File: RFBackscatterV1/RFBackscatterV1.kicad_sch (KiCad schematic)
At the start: 3 parts, among them J1 SMA-J-P-H-RA-TH1, U1 HSWA2-30DR+

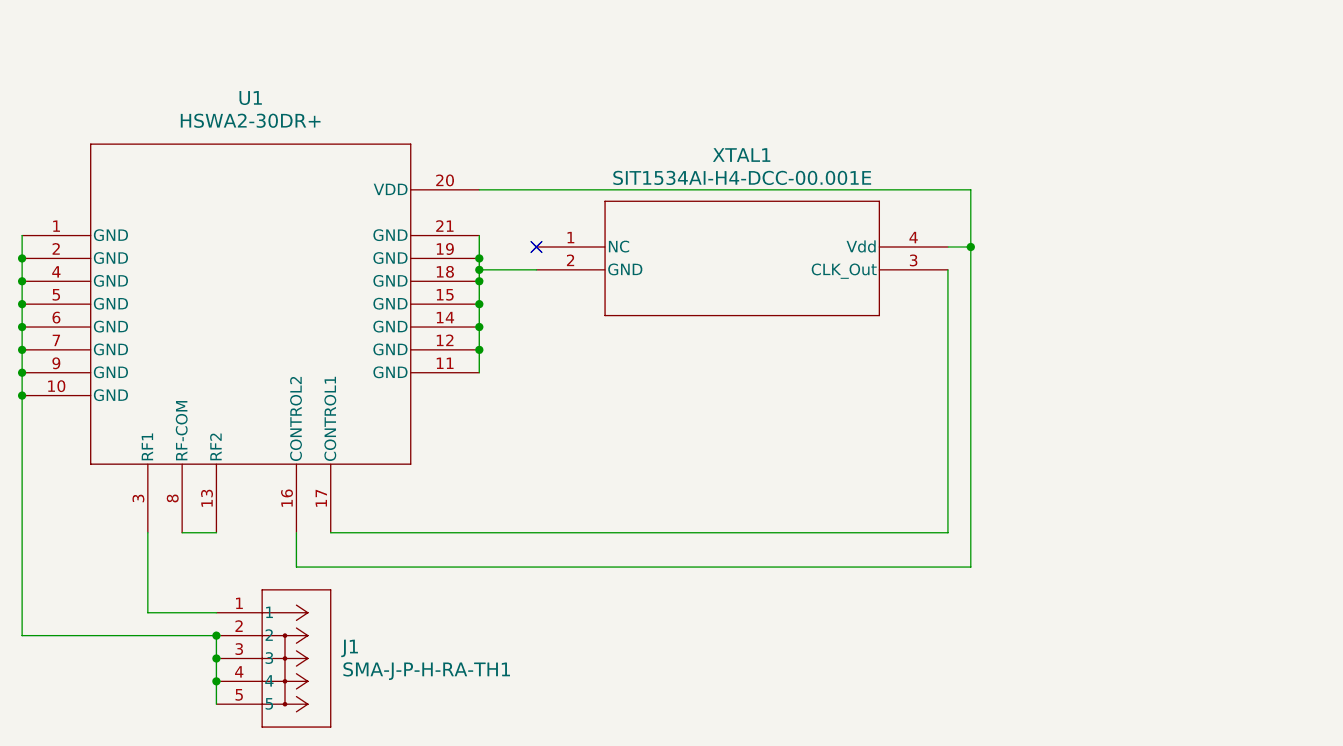
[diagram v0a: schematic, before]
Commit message: Added SKY13351, finished initial schematic
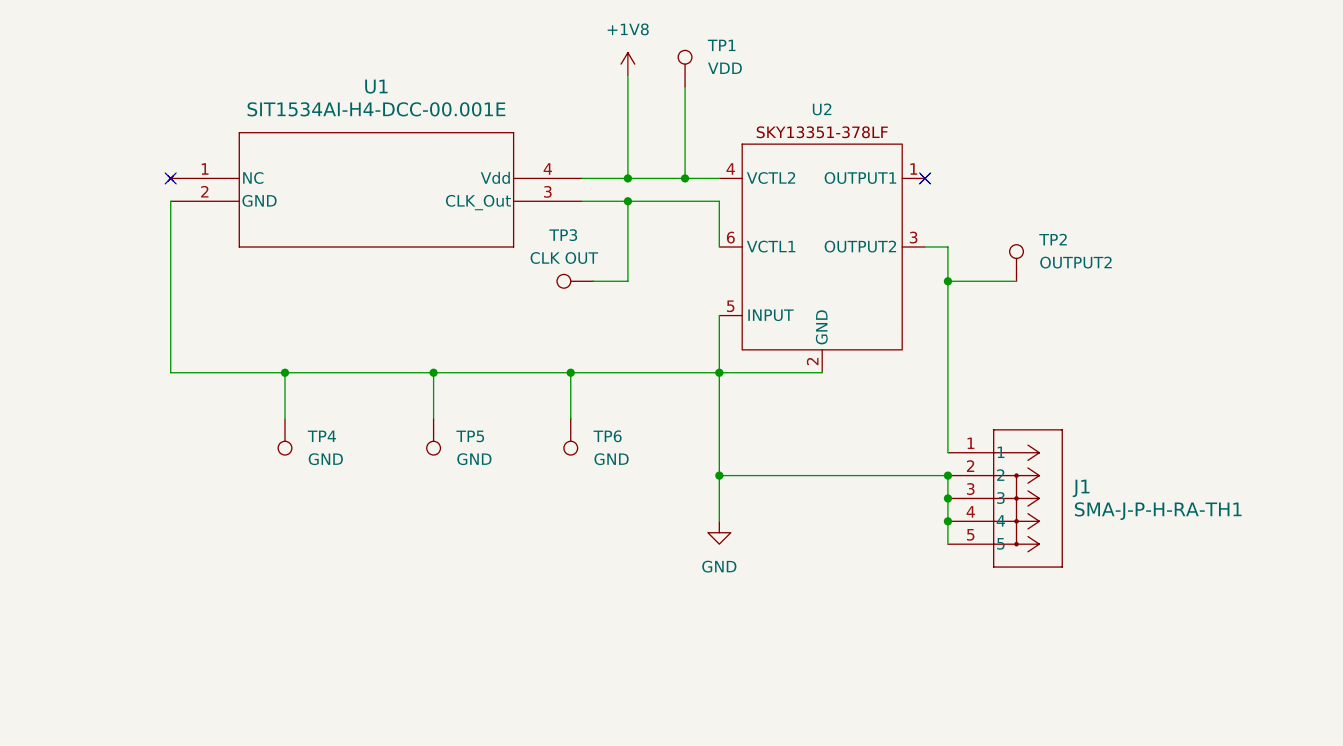
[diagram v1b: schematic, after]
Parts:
- removed U1: HSWA2-30DR+, DG983-1_MNC, symbol 2024-02-16_20-57-40:HSWA2-30DR+
- added TP1: VDD, symbol Connector:TestPoint
- added TP2: OUTPUT2, symbol Connector:TestPoint
- added TP3: CLK OUT, symbol Connector:TestPoint
- added TP4, TP5, TP6: GND, symbol Connector:TestPoint
- added U2: ~, symbol WADAR_KiCAD_Library:SKY13351-378LF
- renumbered XTAL1 to U1
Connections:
- net GND: now reaches U1.2 (GND)
- net GND: now also J1.2, J1.3, J1.4, J1.5, TP4.1, TP5.1, TP6.1, U2.2 (GND), U2.5 (INPUT)
- net at U1.3 (CLK_Out): now also TP3.1, U2.6 (VCTL1)
- net +1V8: now reaches U1.4 (Vdd)
- net +1V8: now also TP1.1, U2.4 (VCTL2)
- net at J1.1: now also TP2.1, U2.3 (OUTPUT2)
- no-connect marks 1 -> 2
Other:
- company: (none) -> UCSC J-Lab
- title: (none) -> RF Backscatter Tag
- moved on the sheet: J1, U1

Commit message: Finished SKY13351 footprint, staged board
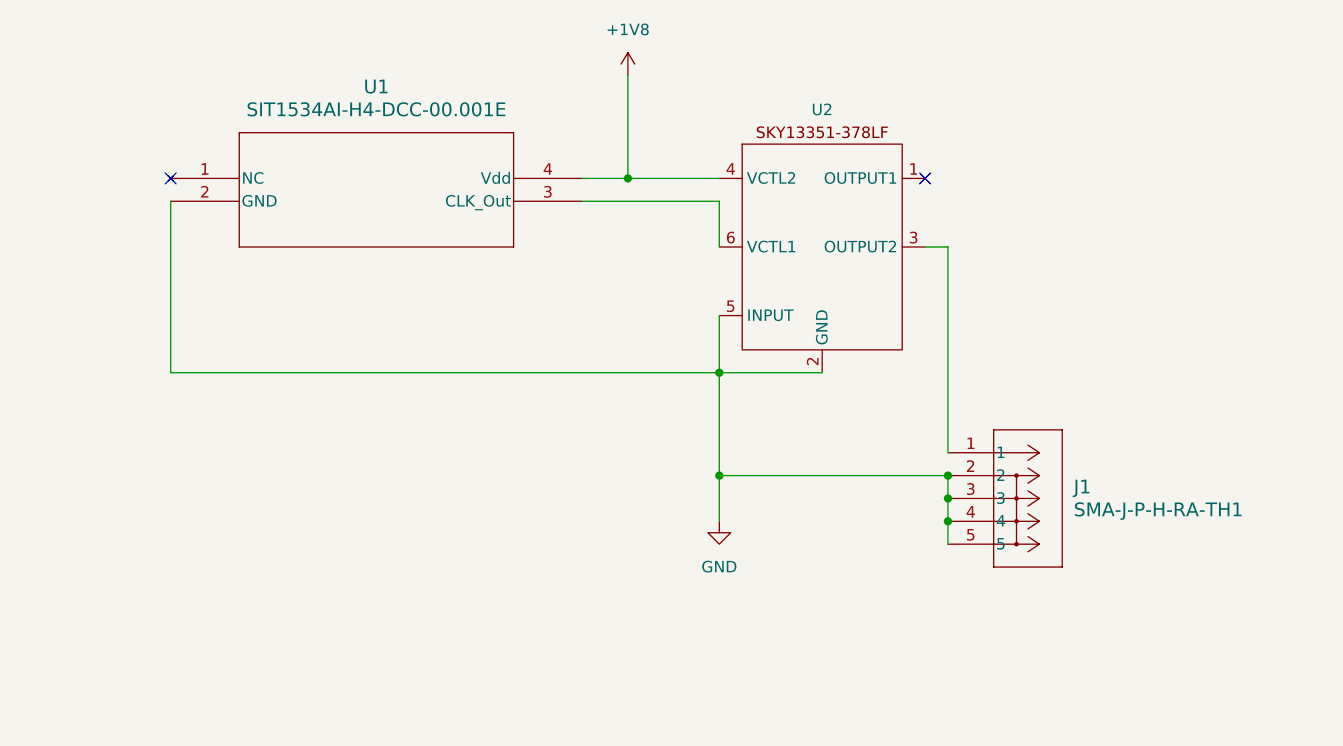
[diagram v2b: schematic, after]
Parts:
- removed TP1: VDD, symbol Connector:TestPoint
- removed TP2: OUTPUT2, symbol Connector:TestPoint
- removed TP3: CLK OUT, symbol Connector:TestPoint
- removed TP4, TP5, TP6: GND, symbol Connector:TestPoint
- U2: footprint (none) -> JLab_FP:SKY13351_FP
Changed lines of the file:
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@@
     (company "UCSC J-Lab")
-  )
-  (junction (at 104.14 101.6) (diameter 0) (color 0 0 0 0)
   )
   (junction (at 177.8 113.03) (diameter 0) (color 0 0 0 0)
   )
   (junction (at 152.4 113.03) (diameter 0) (color 0 0 0 0)
-  )
-  (junction (at 142.24 82.55) (diameter 0) (color 0 0 0 0)
   )
   (junction (at 152.4 101.6) (diameter 0) (color 0 0 0 0)
@@
   (junction (at 142.24 80.01) (diameter 0) (color 0 0 0 0)
   )
-  (junction (at 120.65 101.6) (diameter 0) (color 0 0 0 0)
-  )
-  (junction (at 148.59 80.01) (diameter 0) (color 0 0 0 0)
-  )
   (junction (at 177.8 118.11) (diameter 0) (color 0 0 0 0)
-  )
-  (junction (at 177.8 91.44) (diameter 0) (color 0 0 0 0)
-  )
-  (junction (at 135.89 101.6) (diameter 0) (color 0 0 0 0)
   )
   (no_connect (at 175.26 80.01))
   (no_connect (at 91.44 80.01))
-  (wire (pts (xy 104.14 101.6) (xy 120.65 101.6))
-    (stroke (width 0) (type default))
-  )
-  (wire (pts (xy 135.89 106.68) (xy 135.89 101.6))
-    (stroke (width 0) (type default))
-  )
-  (wire (pts (xy 177.8 87.63) (xy 177.8 91.44))
-    (stroke (width 0) (type default))
-  )
   (wire (pts (xy 152.4 113.03) (xy 152.4 118.11))
     (stroke (width 0) (type default))
@@
     (stroke (width 0) (type default))
   )
-  (wire (pts (xy 142.24 82.55) (xy 152.4 82.55))
+  (wire (pts (xy 137.16 82.55) (xy 152.4 82.55))
     (stroke (width 0) (type default))
   )
   (wire (pts (xy 142.24 68.58) (xy 142.24 80.01))
-    (stroke (width 0) (type default))
-  )
-  (wire (pts (xy 142.24 91.44) (xy 138.43 91.44))
     (stroke (width 0) (type default))
   )
@@
     (stroke (width 0) (type default))
   )
-  (wire (pts (xy 120.65 101.6) (xy 135.89 101.6))
-    (stroke (width 0) (type default))
-  )
   (wire (pts (xy 152.4 101.6) (xy 152.4 113.03))
     (stroke (width 0) (type default))
   )
-  (wire (pts (xy 120.65 101.6) (xy 120.65 106.68))
-    (stroke (width 0) (type default))
-  )
-  (wire (pts (xy 142.24 80.01) (xy 148.59 80.01))
-    (stroke (width 0) (type default))
-  )
-  (wire (pts (xy 104.14 101.6) (xy 104.14 106.68))
+  (wire (pts (xy 142.24 80.01) (xy 152.4 80.01))
     (stroke (width 0) (type default))
   )
@@
     (stroke (width 0) (type default))
   )
-  (wire (pts (xy 91.44 101.6) (xy 104.14 101.6))
-    (stroke (width 0) (type default))
-  )
-  (wire (pts (xy 148.59 69.85) (xy 148.59 80.01))
+  (wire (pts (xy 91.44 101.6) (xy 152.4 101.6))
     (stroke (width 0) (type default))
   )
@@
     (stroke (width 0) (type default))
   )
-  (wire (pts (xy 177.8 91.44) (xy 177.8 110.49))
+  (wire (pts (xy 177.8 87.63) (xy 177.8 110.49))
     (stroke (width 0) (type default))
   )
   (wire (pts (xy 152.4 82.55) (xy 152.4 87.63))
     (stroke (width 0) (type default))
-  )
-  (wire (pts (xy 142.24 82.55) (xy 142.24 91.44))
-    (stroke (width 0) (type default))
-  )
-  (wire (pts (xy 177.8 91.44) (xy 185.42 91.44))
-    (stroke (width 0) (type default))
-  )
-  (wire (pts (xy 135.89 101.6) (xy 152.4 101.6))
-    (stroke (width 0) (type default))
-  )
-  (wire (pts (xy 137.16 82.55) (xy 142.24 82.55))
-    (stroke (width 0) (type default))
-  )
-  (wire (pts (xy 148.59 80.01) (xy 152.4 80.01))
-    (stroke (width 0) (type default))
-  )
-  (symbol (lib_id "Connector:TestPoint") (at 185.42 91.44 0) (unit 1)
-    (in_bom yes) (on_board yes) (dnp no) (fields_autoplaced)
-    (property "Reference" "TP2" (at 187.96 86.868 0)
-      (effects (font (size 1.27 1.27)) (justify left))
-    )
-    (property "Value" "OUTPUT2" (at 187.96 89.408 0)
-      (effects (font (size 1.27 1.27)) (justify left))
-    )
-    (property "Footprint" "" (at 190.5 91.44 0)
-      (effects (font (size 1.27 1.27)) hide)
-    )
-    (property "Datasheet" "~" (at 190.5 91.44 0)
-      (effects (font (size 1.27 1.27)) hide)
-    )
-    (pin "1")
-    (instances
-      (project "RFBackscatterV1"
-        (path "/1b480a55-1292-4321-8fce-0463cf94490c"
-          (reference "TP2") (unit 1)
-        )
-      )
-    )
-  )
-  (symbol (lib_id "Connector:TestPoint") (at 138.43 91.44 90) (unit 1)
-    (in_bom yes) (on_board yes) (dnp no) (fields_autoplaced)
-    (property "Reference" "TP3" (at 135.128 86.36 90)
-      (effects (font (size 1.27 1.27)))
-    )
-    (property "Value" "CLK OUT" (at 135.128 88.9 90)
-      (effects (font (size 1.27 1.27)))
-    )
-    (property "Footprint" "" (at 138.43 86.36 0)
-      (effects (font (size 1.27 1.27)) hide)
-    )
-    (property "Datasheet" "~" (at 138.43 86.36 0)
-      (effects (font (size 1.27 1.27)) hide)
-    )
-    (pin "1")
-    (instances
-      (project "RFBackscatterV1"
-        (path "/1b480a55-1292-4321-8fce-0463cf94490c"
-          (reference "TP3") (unit 1)
-        )
-      )
-    )
-  )
-  (symbol (lib_id "Connector:TestPoint") (at 104.14 106.68 180) (unit 1)
-    (in_bom yes) (on_board yes) (dnp no) (fields_autoplaced)
-    (property "Reference" "TP4" (at 106.68 108.712 0)
-      (effects (font (size 1.27 1.27)) (justify right))
-    )
-    (property "Value" "GND" (at 106.68 111.252 0)
-      (effects (font (size 1.27 1.27)) (justify right))
-    )
-    (property "Footprint" "" (at 99.06 106.68 0)
-      (effects (font (size 1.27 1.27)) hide)
-    )
-    (property "Datasheet" "~" (at 99.06 106.68 0)
-      (effects (font (size 1.27 1.27)) hide)
-    )
-    (pin "1")
-    (instances
-      (project "RFBackscatterV1"
-        (path "/1b480a55-1292-4321-8fce-0463cf94490c"
-          (reference "TP4") (unit 1)
-        )
-      )
-    )
   )
   (symbol (lib_id "WADAR_KiCAD_Library:SKY13351-378LF") (at 163.83 82.55 0) (unit 1)
@@
       (effects (font (size 1.27 1.27)) hide)
     )
-    (property "Footprint" "" (at 149.86 72.39 0)
+    (property "Footprint" "JLab_FP:SKY13351_FP" (at 149.86 72.39 0)
       (effects (font (size 1.27 1.27)) hide)
     )
@@
         (path "/1b480a55-1292-4321-8fce-0463cf94490c"
           (reference "U2") (unit 1)
-        )
-      )
-    )
-  )
-  (symbol (lib_id "Connector:TestPoint") (at 120.65 106.68 180) (unit 1)
-    (in_bom yes) (on_board yes) (dnp no) (fields_autoplaced)
-    (property "Reference" "TP5" (at 123.19 108.712 0)
-      (effects (font (size 1.27 1.27)) (justify right))
-    )
-    (property "Value" "GND" (at 123.19 111.252 0)
-      (effects (font (size 1.27 1.27)) (justify right))
-    )
-    (property "Footprint" "" (at 115.57 106.68 0)
-      (effects (font (size 1.27 1.27)) hide)
-    )
-    (property "Datasheet" "~" (at 115.57 106.68 0)
-      (effects (font (size 1.27 1.27)) hide)
-    )
-    (pin "1")
-    (instances
-      (project "RFBackscatterV1"
-        (path "/1b480a55-1292-4321-8fce-0463cf94490c"
-          (reference "TP5") (unit 1)
         )
       )
@@
         )
       )
-    )
-  )
-  (symbol (lib_id "Connector:TestPoint") (at 135.89 106.68 180) (unit 1)
-    (in_bom yes) (on_board yes) (dnp no) (fields_autoplaced)
-    (property "Reference" "TP6" (at 138.43 108.712 0)
-      (effects (font (size 1.27 1.27)) (justify right))
-    )
-    (property "Value" "GND" (at 138.43 111.252 0)
-      (effects (font (size 1.27 1.27)) (justify right))
-    )
-    (property "Footprint" "" (at 130.81 106.68 0)
-      (effects (font (size 1.27 1.27)) hide)
-    )
-    (property "Datasheet" "~" (at 130.81 106.68 0)
-      (effects (font (size 1.27 1.27)) hide)
-    )
-    (pin "1")
-    (instances
-      (project "RFBackscatterV1"
-        (path "/1b480a55-1292-4321-8fce-0463cf94490c"
-          (reference "TP6") (unit 1)
-        )
-      )
-    )
-  )
-  (symbol (lib_id "Connector:TestPoint") (at 148.59 69.85 0) (unit 1)
-    (in_bom yes) (on_board yes) (dnp no) (fields_autoplaced)
-    (property "Reference" "TP1" (at 151.13 65.278 0)
-      (effects (font (size 1.27 1.27)) (justify left))
-    )
-    (property "Value" "VDD" (at 151.13 67.818 0)
-      (effects (font (size 1.27 1.27)) (justify left))
-    )
-    (property "Footprint" "" (at 153.67 69.85 0)
-      (effects (font (size 1.27 1.27)) hide)
-    )
-    (property "Datasheet" "~" (at 153.67 69.85 0)
-      (effects (font (size 1.27 1.27)) hide)
-    )
-    (pin "1")
-    (instances
-      (project "RFBackscatterV1"
-        (path "/1b480a55-1292-4321-8fce-0463cf94490c"
-          (reference "TP1") (unit 1)
-        )
-      )
